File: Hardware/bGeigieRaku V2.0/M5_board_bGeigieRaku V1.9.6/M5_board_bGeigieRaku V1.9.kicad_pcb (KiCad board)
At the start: 2 copper layers, 129.4 x 64.6 mm, 30 parts, among them J1 M5 2x15 pin, J10 QI GND, J11 QI charger Plus, J12 Geiger, J2 Geiger, J3 GPS, J7 Conn_01x14_Female, J8 QI charger GND, J9 QI Plus, Q1 IRF4905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

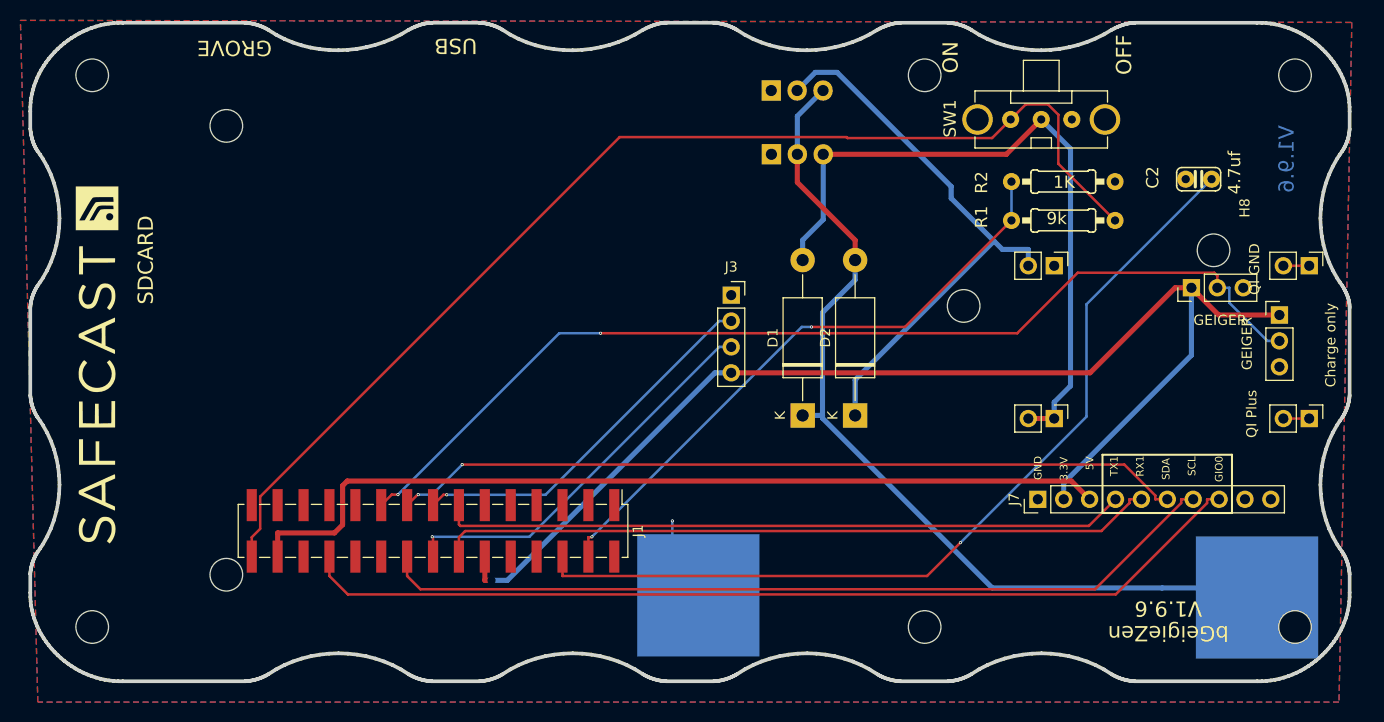
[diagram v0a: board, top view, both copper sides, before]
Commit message: Made changes on board after new V1.9.6 came back
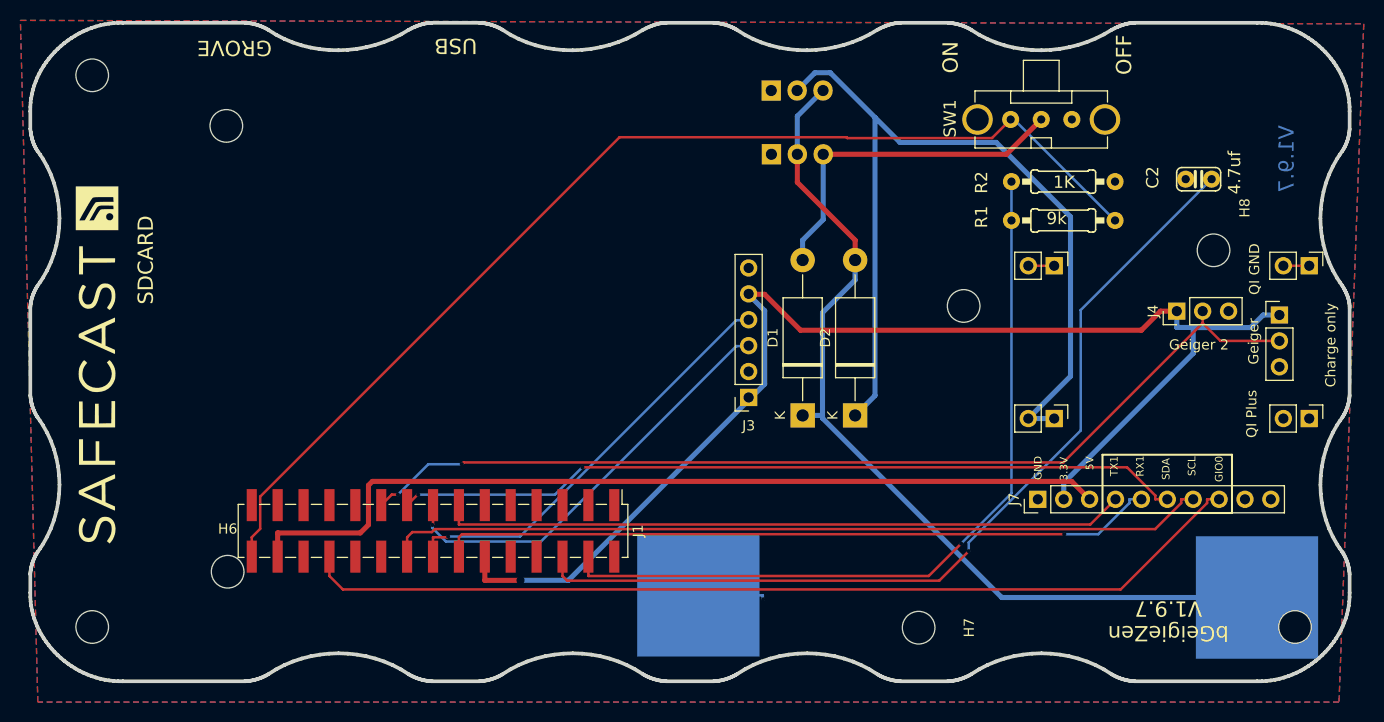
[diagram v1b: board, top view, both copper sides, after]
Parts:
- removed the G*** at (178.2, 123.1)
- removed H10, H11 (x2), H9: MountingHole_Pad, MountingHole:MountingHole_3.2mm_M3
- removed J12: Geiger, Connector_PinHeader_2.54mm:PinHeader_1x03_P2.54mm_Vertical
- added H6: MountingHole_Pad, MountingHole:MountingHole_3.2mm_M3, F.Cu at (103.9, 120.5)
- added H7: MountingHole_Pad, MountingHole:MountingHole_3.2mm_M3, F.Cu at (171.7, 126.0)
- added J4: Geiger 2, Connector_PinHeader_2.54mm:PinHeader_1x03_P2.54mm_Vertical, F.Cu at (197.0, 95.0)
- J3: footprint Connector_PinSocket_2.54mm:PinSocket_1x04_P2.54mm_Vertical -> Connector_PinSocket_2.54mm:PinSocket_1x06_P2.54mm_Vertical
- moved J3 10.2 mm to (155.0, 103.4), turned to 180 degrees
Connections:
- D2 pad 1: Net-(D2-Pad1) -> Net-(J11-Pad1)
- J10 pad 1: Net-(J10-Pad1) -> GND
- J10 pad 2: Net-(J10-Pad1) -> GND
- J11 pad 1: /VBATT -> Net-(J11-Pad1)
- J11 pad 2: /VBATT -> Net-(J11-Pad1)
- J3 pad 1: GND -> unconnected-(J3-Pad1)
- J3 pad 2: /TX2 -> GND
- J3 pad 3: /RX2 -> /TX2
- J3 pad 4: 3.3V -> /RX2
- J8 pad 2: Net-(D2-Pad1) -> GND
- Q1 pad 2: Net-(D2-Pad1) -> Net-(J11-Pad1)
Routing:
- net Net-(J11-Pad1): track 0.00 -> 87.5 mm
- net Net-(D2-Pad1): track 55.6 -> 0.00 mm
- net /VBATT: track 67.7 -> 34.0 mm
- net Net-(J1-Pad4): track 60.1 -> 77.3 mm, vias 2 -> 1
- net 3.3V: track 119.2 -> 125.8 mm
- net /TX2: track 36.7 -> 41.8 mm
- net /GIO2: track 101.9 -> 97.4 mm
- net Net-(J1-Pad30): track 113.6 -> 109.6 mm
- net Net-(BT1-Pad1): track 85.8 -> 88.7 mm
- net GND: track 6.37 -> 9.27 mm
- net /SCL: track 83.4 -> 80.8 mm
- net /RX2: track 39.0 -> 41.6 mm
- net Net-(J10-Pad1): track 2.54 -> 0.00 mm
- net /Reset: track 88.1 -> 89.5 mm
- net /RX1: vias 0 -> 1
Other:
- board text added: "Notes 2021-03-09 for V1.9.7 - check power track width - Remake warning lable - realign the holes for M5Stack mounts - check alignments all holes"
- board text added: "V1.9.7"
- board text added: "bGeigieZen V1.9.7"
- board text removed: "V1.9.6"
- board text removed: "bGeigieZen V1.9.6"

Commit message: Updated to V1.9.7
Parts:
- BT1: footprint Battery_Holders:BATTERY_18650-HOLDER -> Library:BATTERY_18650-HOLDER
- moved J7 22.9 mm to (160.5, 111.7)
- moved D1 3.43 mm to (161.4, 101.9)
- moved D2 3.43 mm to (166.6, 101.9)
- moved BT1 3.00 mm to (177.7, 120.0)
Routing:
- net Net-(J11-Pad1): track 87.5 -> 54.8 mm
- net 5V: track 87.1 -> 63.9 mm, vias 0 -> 1
- net /TX1: track 67.3 -> 44.5 mm
- net /SDA: track 77.6 -> 55.3 mm, vias 2 -> 0
- net /RX1: track 70.6 -> 48.4 mm
- net /SCL: track 80.8 -> 58.6 mm
- net /GIO0: track 93.6 -> 72.0 mm
- net 3.3V: track 125.8 -> 114.8 mm
- net GND: track 9.27 -> 3.11 mm, vias 1 -> 0
- net /VBATT: track 34.0 -> 30.3 mm
- net /Reset: track 89.5 -> 85.9 mm, vias 1 -> 2
- net /RX2: track 41.6 -> 44.9 mm
- net /TX2: track 41.8 -> 38.6 mm
- net Net-(J1-Pad4): track 77.3 -> 75.0 mm
- net Net-(BT1-Pad1): track 88.7 -> 90.9 mm
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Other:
- board text added: "Notes 2021-03-09 for V1.9.7 - check power track width - Remake warning lable - realign the holes for M5Stack mounts - check alignments all holes - battery need to move more to the center of the board - battery holder must be trough holes"
- board text removed: "Notes 2021-03-09 for V1.9.7 - check power track width - Remake warning lable - realign the holes for M5Stack mounts - check alignments all holes"
- board text removed: "V1.9.7"

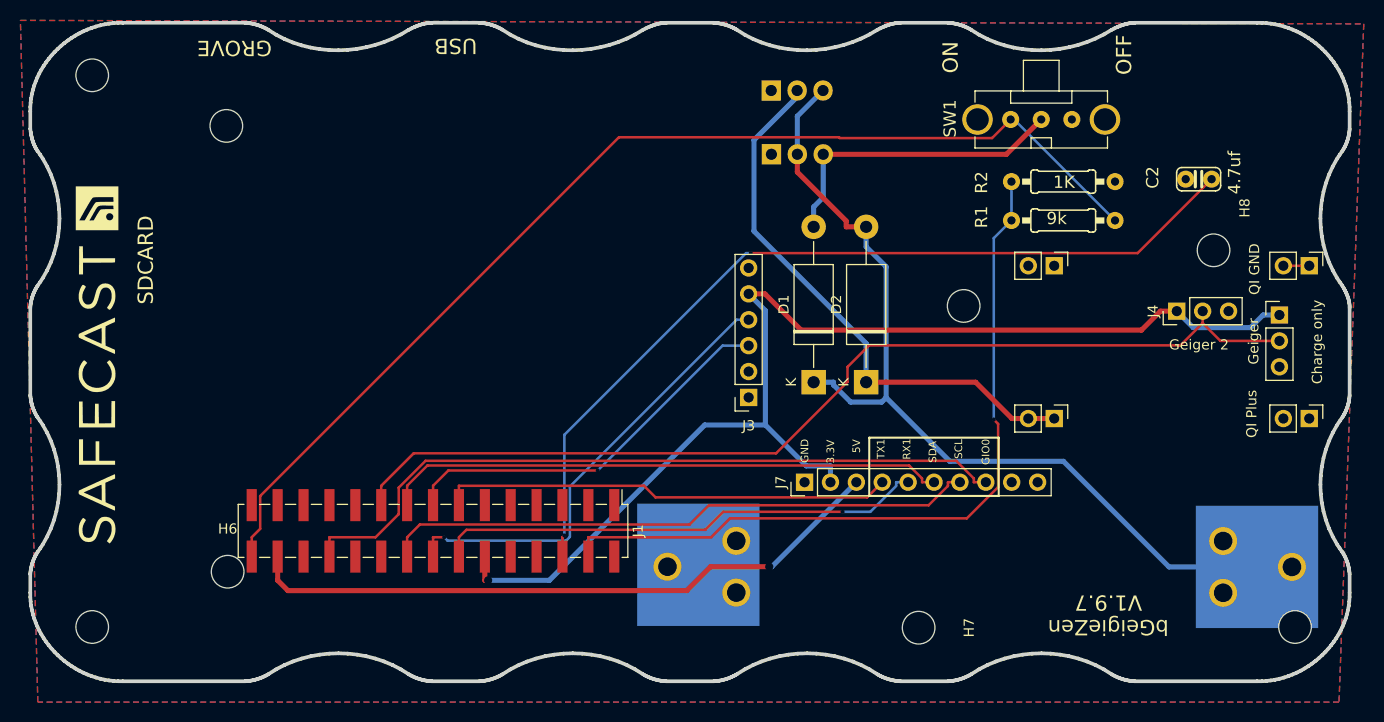
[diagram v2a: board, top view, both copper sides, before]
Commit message: Mirrored pins of M5connector, used smaller diodes.
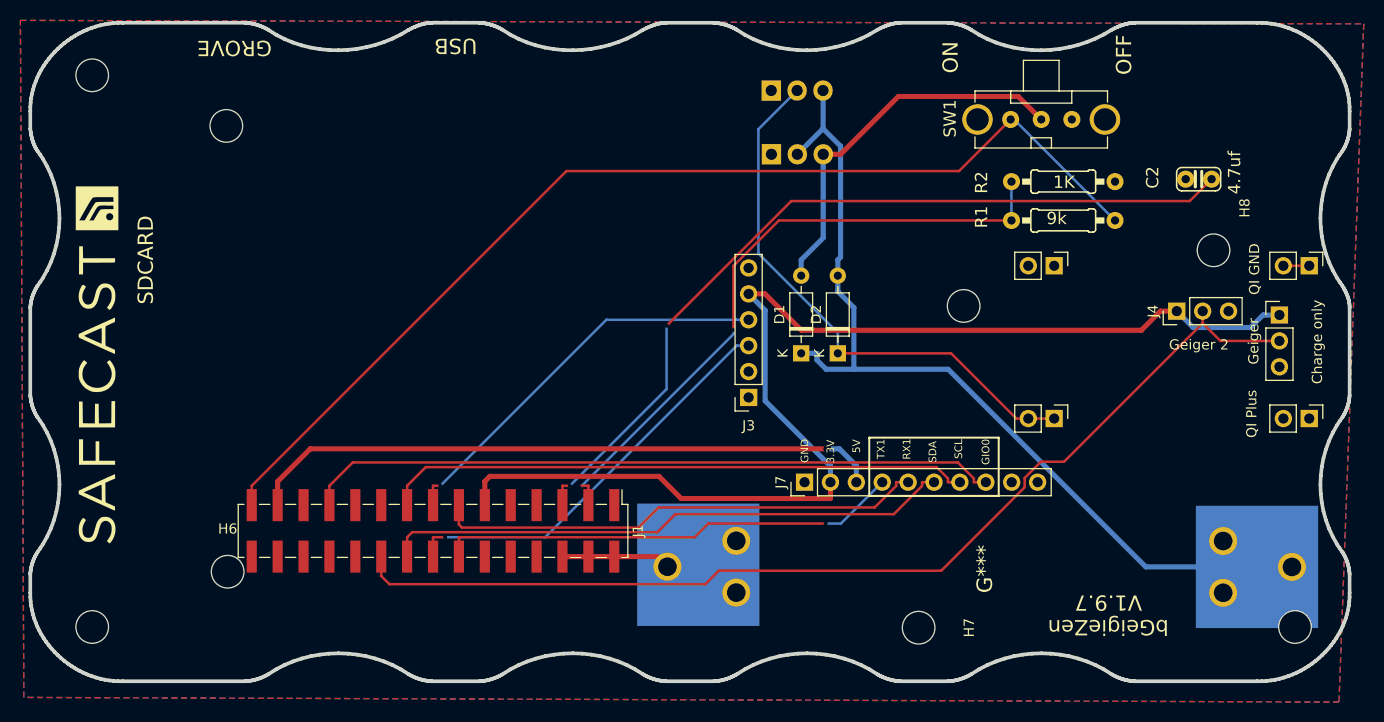
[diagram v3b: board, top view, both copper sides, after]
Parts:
- added G***: LOGO, bGeigieRaku_M5_1015:18650 map, B.Cu at (178.2, 120.2)
- D1, D2: footprint Diode_THT:D_DO-15_P15.24mm_Horizontal -> Diode_THT:D_DO-35_SOD27_P7.62mm_Horizontal
- moved D2 3.97 mm to (163.8, 99.1)
- moved D1 3.08 mm to (160.2, 99.1)
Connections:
- J1 pad 1: GND -> /AD1
- J1 pad 11: unconnected-(J1-Pad11) -> 3.3V
- J1 pad 12: 3.3V -> unconnected-(J1-Pad12)
- J1 pad 13: /TX1 -> /RX1
- J1 pad 14: /RX1 -> /TX1
- J1 pad 15: /TX2 -> /RX2
- J1 pad 16: /RX2 -> /TX2
- J1 pad 17: /SDA -> /SCL
- J1 pad 18: /SCL -> /SDA
- J1 pad 19: /GIO2 -> /GIO5
- J1 pad 2: /AD1 -> GND
- J1 pad 20: /GIO5 -> /GIO2
- J1 pad 21: unconnected-(J1-Pad21) -> /GIO13
- J1 pad 22: /GIO13 -> unconnected-(J1-Pad22)
- J1 pad 23: unconnected-(J1-Pad23) -> /GIO0
- J1 pad 24: /GIO0 -> unconnected-(J1-Pad24)
- J1 pad 25: unconnected-(J1-Pad25) -> /GIO34
- J1 pad 26: /GIO34 -> unconnected-(J1-Pad26)
- J1 pad 27: unconnected-(J1-Pad27) -> 5V
- J1 pad 28: 5V -> unconnected-(J1-Pad28)
- J1 pad 29: unconnected-(J1-Pad29) -> Net-(R1-Pad1)
- J1 pad 3: GND -> Net-(R1-Pad2)
- J1 pad 30: Net-(J1-Pad30) -> unconnected-(J1-Pad30)
- J1 pad 4: Net-(J1-Pad4) -> GND
- J1 pad 5: GND -> /Reset
- J1 pad 6: /Reset -> GND
- R1 pad 1: Net-(J1-Pad30) -> Net-(R1-Pad1)
- R1 pad 2: Net-(J1-Pad4) -> Net-(R1-Pad2)
- R2 pad 1: Net-(J1-Pad4) -> Net-(R1-Pad2)
- SW1 pad 3: Net-(J1-Pad30) -> Net-(R1-Pad1)
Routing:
- net Net-(J1-Pad30): track 109.6 -> 0.00 mm
- net Net-(R1-Pad1): track 0.00 -> 105.6 mm
- net Net-(J1-Pad4): track 75.0 -> 0.00 mm, vias 1 -> 0
- net Net-(R1-Pad2): track 0.00 -> 63.8 mm, vias 0 -> 2
- net GND: track 3.11 -> 13.8 mm
- net /VBATT: track 30.3 -> 37.5 mm
- net /RX2: track 44.9 -> 39.6 mm
- net /Reset: track 85.9 -> 81.7 mm
- net /GIO2: track 99.4 -> 103.4 mm
- net /GIO0: track 72.0 -> 68.2 mm
- net /TX2: track 38.6 -> 40.6 mm
- net 3.3V: track 114.8 -> 116.3 mm, vias 1 -> 0
- net Net-(BT1-Pad1): track 90.9 -> 89.6 mm
- net 5V: track 63.9 -> 62.7 mm
- net /TX1: track 44.5 -> 45.7 mm, vias 0 -> 1
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
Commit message: Moved battery and 18650 graphics
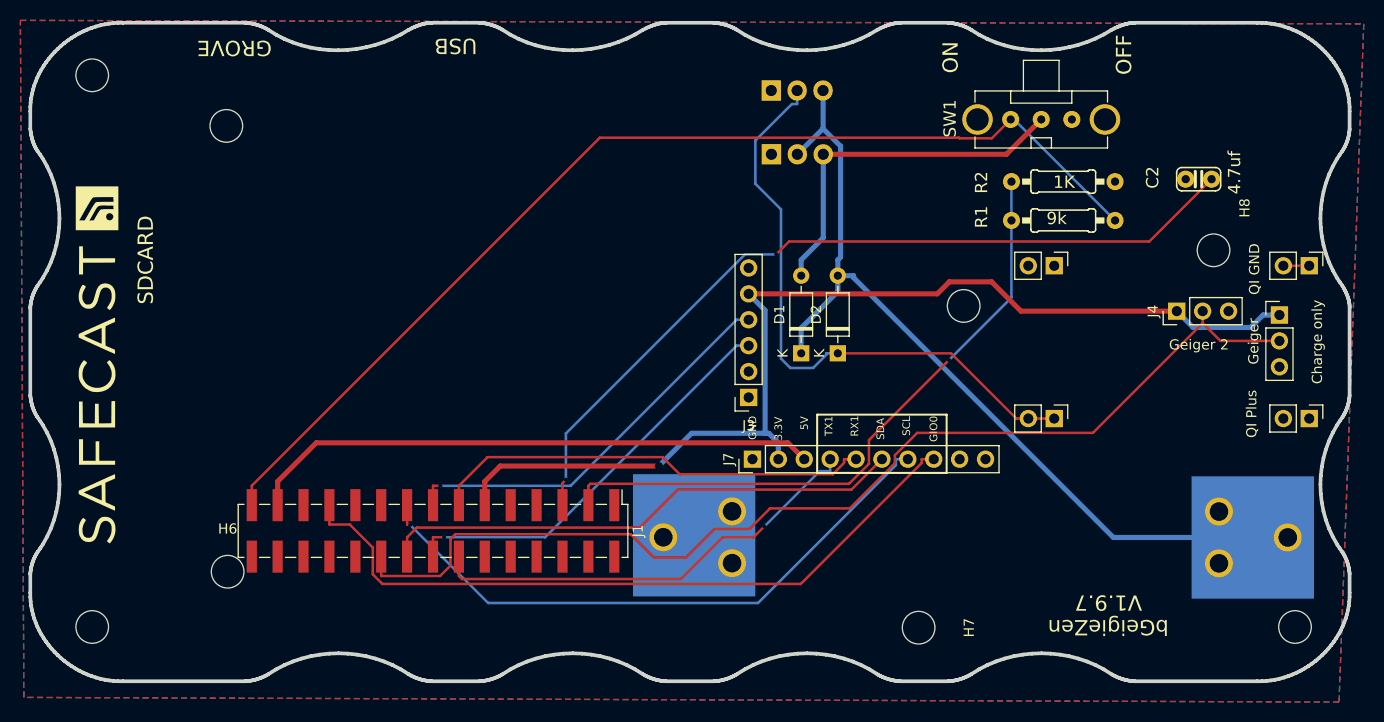
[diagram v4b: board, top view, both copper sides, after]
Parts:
- 18650 picture: renamed from G***
- moved J7 5.59 mm to (155.4, 109.5)
- moved 18650 picture 2.92 mm to (177.8, 117.3)
- moved BT1 2.92 mm to (177.3, 117.1)
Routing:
- net 3.3V: track 116.3 -> 104.3 mm, vias 0 -> 1
- net GND: track 13.8 -> 3.11 mm
- net 5V: track 62.7 -> 56.2 mm, vias 1 -> 0
- net Net-(D2-Pad1): track 54.5 -> 59.8 mm
- net /RX1: track 48.1 -> 43.5 mm
- net /SDA: track 56.0 -> 51.6 mm
- net Net-(BT1-Pad1): track 89.6 -> 86.5 mm
- net /GIO2: track 103.4 -> 106.1 mm
- net /SCL: track 57.7 -> 60.4 mm, vias 0 -> 1
- net /GIO0: track 68.2 -> 70.4 mm
- net /VBATT: track 37.5 -> 35.6 mm
- net /TX1: track 45.7 -> 44.0 mm
- net /Reset: track 81.7 -> 80.8 mm
- net Net-(R1-Pad2): vias 2 -> 1
